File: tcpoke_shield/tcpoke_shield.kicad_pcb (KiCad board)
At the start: 2 copper layers, 25.4 x 20.3 mm, 6 parts, among them P1 CONN_01X05, P3 CONN_01X05

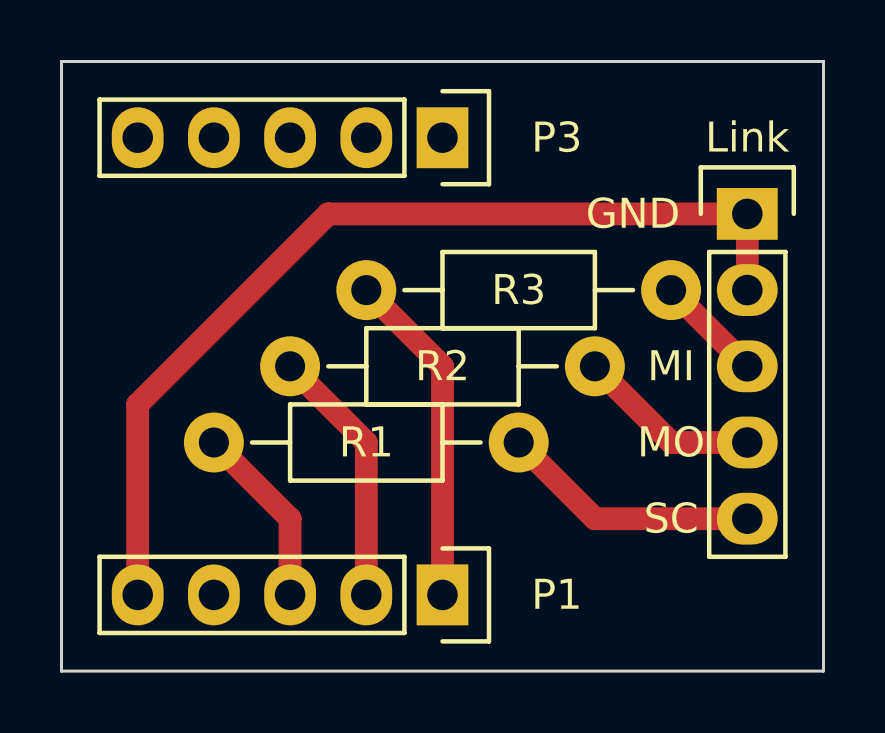
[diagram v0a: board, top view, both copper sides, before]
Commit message: add LED to shield
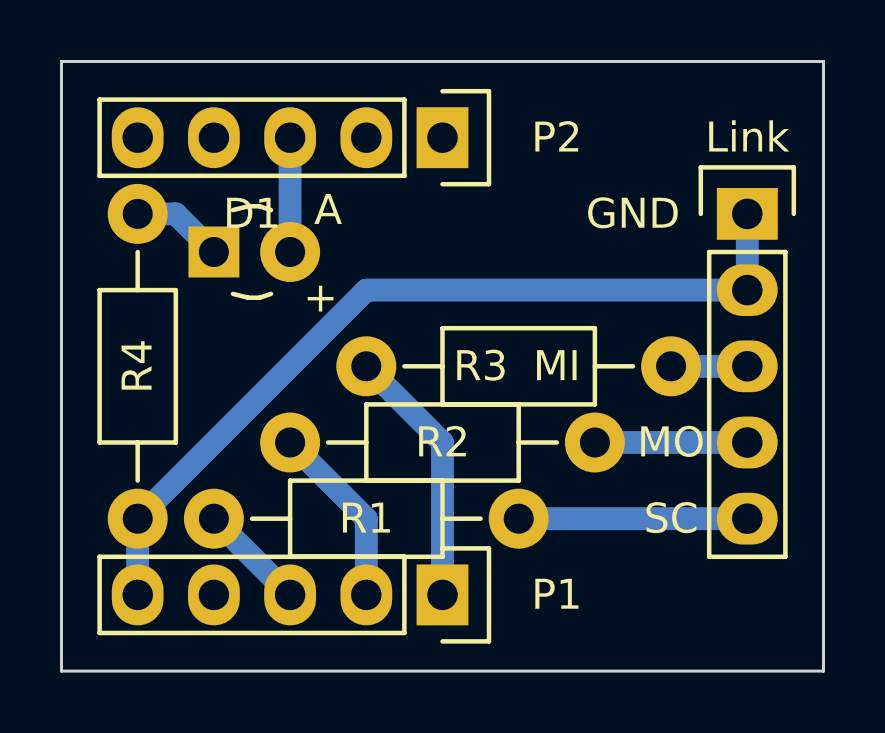
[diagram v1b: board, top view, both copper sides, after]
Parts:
- added D1: LED, Diodes_ThroughHole:Diode_LED_3mm_round_vertical, F.Cu at (149.9, 104.1)
- added R4: 1K, Resistors_ThroughHole:Resistor_Horizontal_RM10mm, F.Cu at (146.1, 108.0)
- moved R1 2.54 mm to (153.7, 113.0)
- moved R3 2.54 mm to (158.8, 108.0)
- moved R2 2.54 mm to (156.2, 110.5)
- renumbered P3 to P2
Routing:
- net Net-(D1-Pad1): track 0.00 -> 3.81 mm
- net Net-(Link1-Pad1): track 31.8 -> 28.6 mm
- net Net-(D1-Pad2): track 0.00 -> 3.07 mm
- net Net-(P1-Pad1): track 11.2 -> 8.67 mm
- net Net-(P1-Pad3): track 6.13 -> 3.59 mm
- net Net-(P1-Pad2): track 8.67 -> 6.13 mm
- net Net-(Link1-Pad3): track 3.59 -> 2.54 mm
- net Net-(Link1-Pad5): track 8.67 -> 7.62 mm
- net Net-(Link1-Pad4): track 6.13 -> 5.08 mm
